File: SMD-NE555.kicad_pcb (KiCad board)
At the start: 2 copper layers, 26.4 x 17.8 mm, 13 parts, among them IC1 NE555D, J1 Conn_01x02_Pin, J2 Conn_01x01_Pin

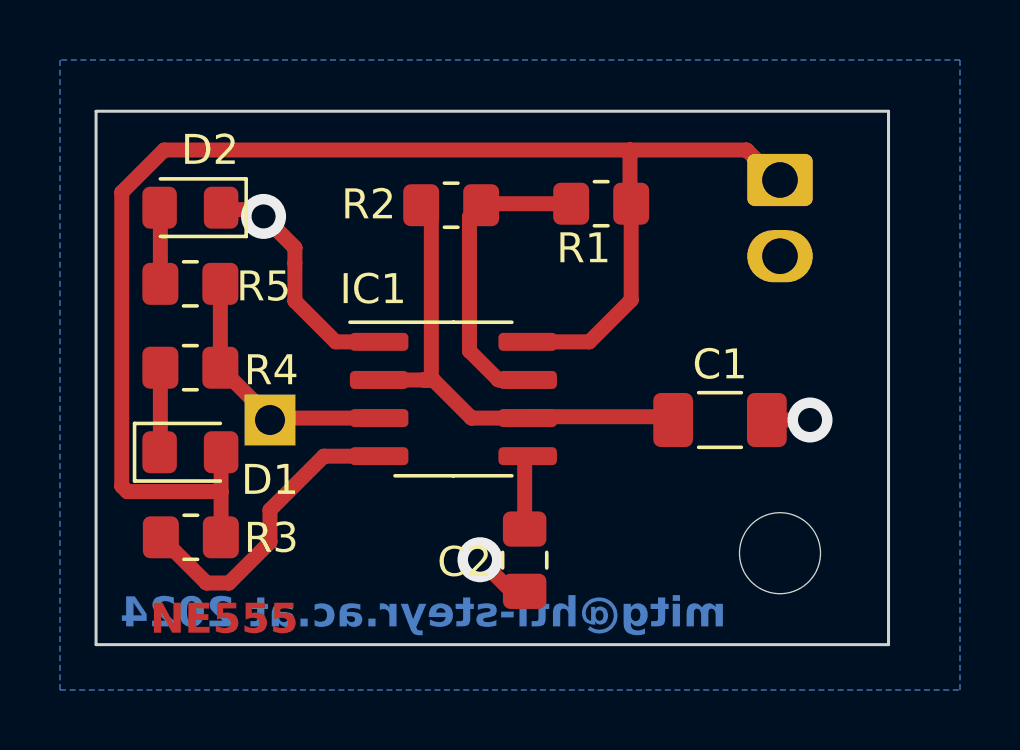
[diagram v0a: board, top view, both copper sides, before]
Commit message: rounded corners gnd plane top&bot
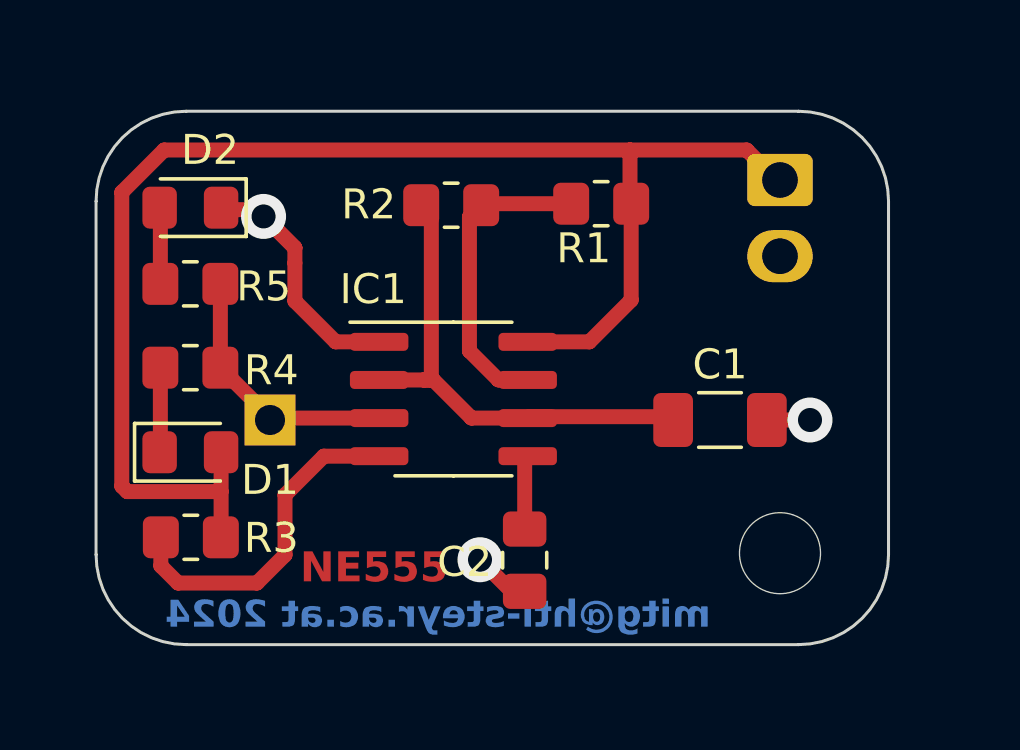
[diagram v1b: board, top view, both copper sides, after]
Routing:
- net Net-(IC1-R): track 10.3 -> 11.4 mm
- added copper zone on F.Cu, net GNDA
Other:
- outline, holes or cut-outs redrawn
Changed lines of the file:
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@@
 				(font
 					(size 1.27 1.27)
+					(thickness 0.15)
 				)
 			)
@@
 				(font
 					(size 1.27 1.27)
+					(thickness 0.15)
 				)
 			)
@@
 				(font
 					(size 1.27 1.27)
+					(thickness 0.15)
 				)
 			)
@@
 				(font
 					(size 1.27 1.27)
+					(thickness 0.15)
 				)
 			)
@@
 				(font
 					(size 1.27 1.27)
+					(thickness 0.15)
 				)
 			)
@@
 				(font
 					(size 1.27 1.27)
+					(thickness 0.15)
 				)
 			)
@@
 				(font
 					(size 1.27 1.27)
+					(thickness 0.15)
 				)
 			)
@@
 				(font
 					(size 1.27 1.27)
+					(thickness 0.15)
 				)
 			)
@@
 				(font
 					(size 1.27 1.27)
+					(thickness 0.15)
 				)
 			)
@@
 				(font
 					(size 1.27 1.27)
+					(thickness 0.15)
 				)
 			)
@@
 				(font
 					(size 1.27 1.27)
+					(thickness 0.15)
 				)
 			)
@@
 				(font
 					(size 1.27 1.27)
+					(thickness 0.15)
 				)
 			)
@@
 				(font
 					(size 1.27 1.27)
+					(thickness 0.15)
 				)
 			)
@@
 				(font
 					(size 1.27 1.27)
+					(thickness 0.15)
 				)
 			)
@@
 				(font
 					(size 1.27 1.27)
+					(thickness 0.15)
 				)
 			)
@@
 				(font
 					(size 1.27 1.27)
+					(thickness 0.15)
 				)
 			)
@@
 				(font
 					(size 1.27 1.27)
+					(thickness 0.15)
 				)
 			)
@@
 				(font
 					(size 1.27 1.27)
+					(thickness 0.15)
 				)
 			)
@@
 				(font
 					(size 1.27 1.27)
+					(thickness 0.15)
 				)
 			)
@@
 				(font
 					(size 1.27 1.27)
+					(thickness 0.15)
 				)
 			)
@@
 				(font
 					(size 1.27 1.27)
+					(thickness 0.15)
 				)
 			)
@@
 				(font
 					(size 1.27 1.27)
+					(thickness 0.15)
 				)
 			)
@@
 				(font
 					(size 1.27 1.27)
+					(thickness 0.15)
 				)
 			)
@@
 				(font
 					(size 1.27 1.27)
+					(thickness 0.15)
 				)
 			)
@@
 				(font
 					(size 1.27 1.27)
+					(thickness 0.15)
 				)
 			)
@@
 				(font
 					(size 1.27 1.27)
+					(thickness 0.15)
 				)
 			)
@@
 				(font
 					(size 1.27 1.27)
+					(thickness 0.15)
 				)
 			)
@@
 				(font
 					(size 1.27 1.27)
+					(thickness 0.15)
 				)
 			)
@@
 				(font
 					(size 1.27 1.27)
+					(thickness 0.15)
 				)
 			)
@@
 				(font
 					(size 1.27 1.27)
+					(thickness 0.15)
 				)
 			)
@@
 				(font
 					(size 1.27 1.27)
+					(thickness 0.15)
 				)
 			)
@@
 				(font
 					(size 1.27 1.27)
+					(thickness 0.15)
 				)
 			)
@@
 				(font
 					(size 1.27 1.27)
+					(thickness 0.15)
 				)
 			)
@@
 				(font
 					(size 1.27 1.27)
+					(thickness 0.15)
 				)
 				(justify mirror)
@@
 				(font
 					(size 1.27 1.27)
+					(thickness 0.15)
 				)
 				(justify mirror)
@@
 				(font
 					(size 1.27 1.27)
+					(thickness 0.15)
 				)
 				(justify mirror)
@@
 				(font
 					(size 1.27 1.27)
+					(thickness 0.15)
 				)
 				(justify mirror)
@@
 				(font
 					(size 1.27 1.27)
+					(thickness 0.15)
 				)
 				(justify mirror)
@@
 				(font
 					(size 1.27 1.27)
+					(thickness 0.15)
 				)
 				(justify mirror)
@@
 		(layer "B.Mask")
 	)
+	(gr_arc
+		(start 95.202 94.488)
+		(mid 93.08068 93.60932)
+		(end 92.202 91.488)
+		(stroke
+			(width 0.1)
+			(type default)
+		)
+		(layer "Edge.Cuts")
+	)
+	(gr_arc
+		(start 118.618 91.488)
+		(mid 117.73932 93.60932)
+		(end 115.618 94.488)
+		(stroke
+			(width 0.1)
+			(type default)
+		)
+		(layer "Edge.Cuts")
+	)
 	(gr_line
-		(start 118.618 94.488)
-		(end 92.202 94.488)
+		(start 115.618 94.488)
+		(end 95.202 94.488)
+		(stroke
+			(width 0.1)
+			(type default)
+		)
+		(layer "Edge.Cuts")
+	)
+	(gr_arc
+		(start 92.202 79.708)
+		(mid 93.08068 77.58668)
+		(end 95.202 76.708)
+		(stroke
+			(width 0.1)
+			(type default)
+		)
+		(layer "Edge.Cuts")
+	)
+	(gr_arc
+		(start 115.618 76.708)
+		(mid 117.73932 77.58668)
+		(end 118.618 79.708)
 		(stroke
 			(width 0.1)
@@
 	)
 	(gr_line
-		(start 92.202 76.708)
-		(end 118.618 76.708)
+		(start 95.202 76.708)
+		(end 115.618 76.708)
 		(stroke
 			(width 0.1)
@@
 	)
 	(gr_line
-		(start 92.202 94.488)
-		(end 92.202 76.708)
+		(start 92.202 91.488)
+		(end 92.202 79.708)
 		(stroke
 			(width 0.1)
@@
 	)
 	(gr_line
-		(start 118.618 76.708)
-		(end 118.618 94.488)
+		(start 118.618 79.708)
+		(end 118.618 91.488)
 		(stroke
 			(width 0.1)
@@
 	)
 	(gr_text "NE555\n"
-		(at 94.0035 94.2125 0)
-		(layer "F.Cu")
+		(at 99 92.5 0)
+		(layer "F.Cu" knockout)
 		(effects
 			(font
@@
 	)
 	(gr_text "mitg@htl-steyr.ac.at 2024\n"
-		(at 93 94 0)
+		(at 94.5 94 0)
 		(layer "B.Cu" knockout)
 		(effects
 			(font
-				(size 1 1)
+				(size 0.9 0.9)
 				(thickness 0.2)
 				(bold yes)
@@
 	)
 	(segment
-		(start 96.634378 92.4345)
-		(end 95.8855 92.4345)
+		(start 97.5655 92.4345)
+		(end 94.9345 92.4345)
 		(width 0.5)
 		(layer "F.Cu")
@@
 	)
 	(segment
-		(start 101.6395 88.2055)
-		(end 99.7945 88.2055)
+		(start 94.3615 91.8615)
+		(end 94.3615 90.9105)
 		(width 0.5)
 		(layer "F.Cu")
@@
 	(segment
 		(start 99.7945 88.2055)
-		(end 98 90)
+		(end 98.5 89.5)
 		(width 0.5)
 		(layer "F.Cu")
@@
 	)
 	(segment
-		(start 98 91.068878)
-		(end 96.634378 92.4345)
+		(start 101.6395 88.2055)
+		(end 99.7945 88.2055)
 		(width 0.5)
 		(layer "F.Cu")
@@
 	)
 	(segment
-		(start 98 90)
-		(end 98 91.068878)
+		(start 98.5 91.5)
+		(end 97.5655 92.4345)
 		(width 0.5)
 		(layer "F.Cu")
@@
 	)
 	(segment
-		(start 95.8855 92.4345)
-		(end 94.3615 90.9105)
+		(start 94.9345 92.4345)
+		(end 94.3615 91.8615)
+		(width 0.5)
+		(layer "F.Cu")
+		(net 7)
+	)
+	(segment
+		(start 98.5 89.5)
+		(end 98.5 91.5)
 		(width 0.5)
 		(layer "F.Cu")
@@
 		(net 2)
 		(net_name "GNDA")
-		(layer "B.Cu")
+		(layers "F&B.Cu")
 		(hatch edge 0.5)
 		(connect_pads
@@
 		(polygon
 			(pts
-				(xy 91 75) (xy 91 96) (xy 121 96) (xy 121 75)
+				(arc
+					(start 95.202 76.708)
+					(mid 93.08068 77.58668)
+					(end 92.202 79.708)
+				)
+				(arc
+					(start 92.202 91.488)
+					(mid 93.08068 93.60932)
+					(end 95.202 94.488)
+				)
+				(arc
+					(start 115.618 94.488)
+					(mid 117.73932 93.60932)
+					(end 118.618 91.488)
+				)
+				(arc
+					(start 118.618 79.708)
+					(mid 117.73932 77.58668)
+					(end 115.618 76.708)
+				)
 			)
 		)

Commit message: molex to pinheader2.54 1x02
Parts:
- J1: footprint Connector_Molex:Molex_KK-254_AE-6410-02A_1x02_P2.54mm_Vertical -> Connector_PinHeader_2.54mm:PinHeader_1x02_P2.54mm_Vertical
- turned J1 to 180 degrees
